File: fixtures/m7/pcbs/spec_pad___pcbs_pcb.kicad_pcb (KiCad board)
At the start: 2 copper layers, 3 parts

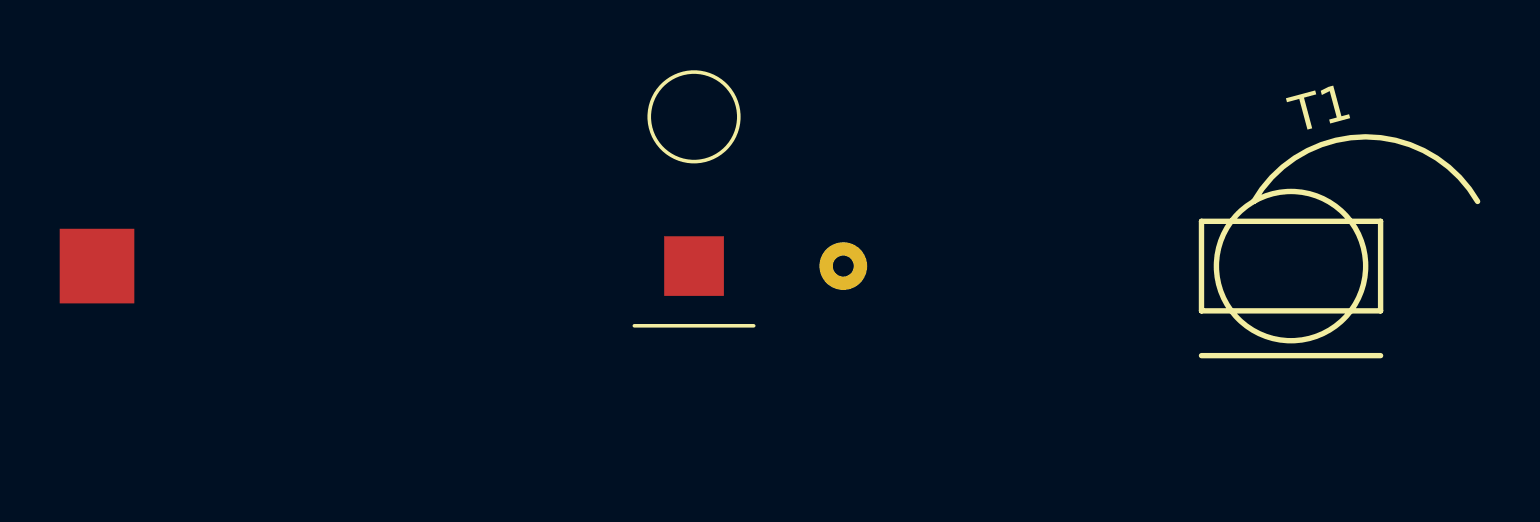
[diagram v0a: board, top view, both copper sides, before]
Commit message: Expand footprint specs and add JS footprints plan
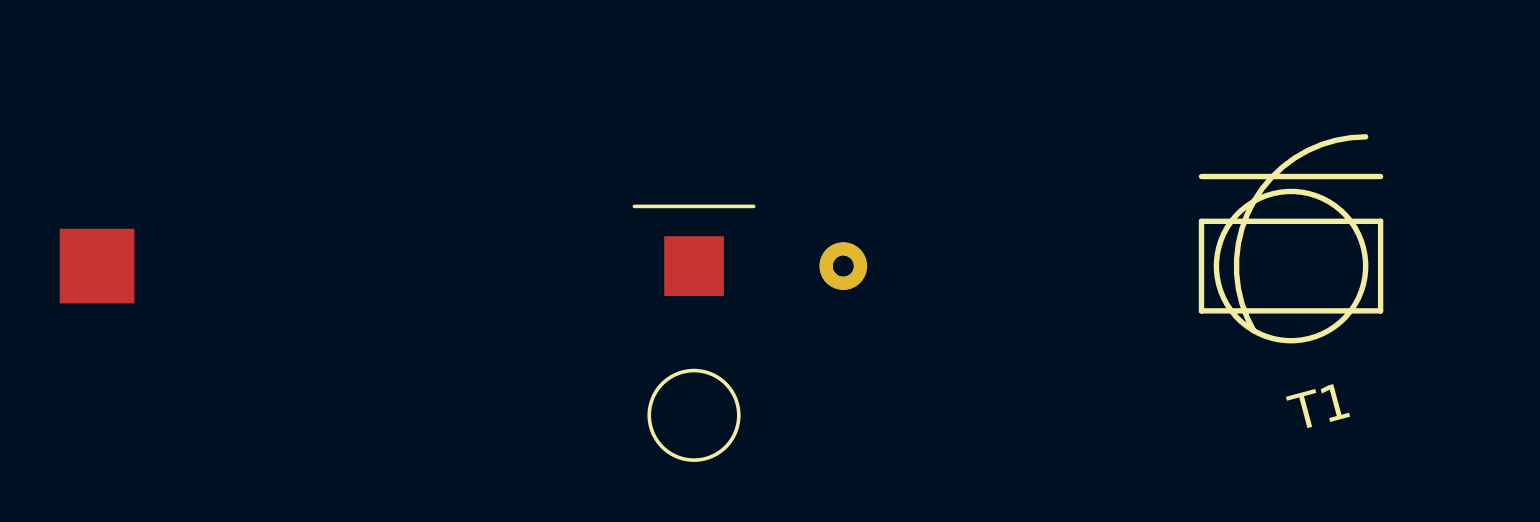
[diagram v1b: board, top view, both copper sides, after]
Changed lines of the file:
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@@
             (fp_text reference "FP1" (at 0 0) (layer F.SilkS) hide (effects (font (size 1.27 1.27) (thickness 0.15))))
             (fp_text value "" (at 0 0) (layer F.SilkS) hide (effects (font (size 1.27 1.27) (thickness 0.15))))
-            (pad 1 smd rect (at 0 0 0) (size 2.5 2.5) (layers F.Cu F.Mask) (net 1 "GND"))
+            (pad 1 smd rect (at 0 0) (size 2.5 2.5) (layers F.Cu F.Mask) (net 1 "GND"))
         )
         (module pad_primitives (layer F.Cu)
@@
             (fp_text reference "FP2" (at 0 0) (layer F.SilkS) hide (effects (font (size 1.27 1.27) (thickness 0.15))))
             (fp_text value "" (at 0 0) (layer F.SilkS) hide (effects (font (size 1.27 1.27) (thickness 0.15))))
-            (pad 1 smd rect (at 0 0 0) (size 2 2) (layers F.Cu F.Mask) (net 2 "VCC"))
-            (pad 2 thru_hole circle (at 5 0 0) (size 1.6 1.6) (drill 0.7) (layers F.Cu B.Cu F.Mask B.Mask) (net 2 "VCC"))
-            (fp_circle (center 0 -5) (end 1.5 -5) (layer F.SilkS) (width 0.12))
-            (fp_line (start -2 2) (end 2 2) (layer F.SilkS) (width 0.12))
+            (pad 1 smd rect (at 0 0) (size 2 2) (layers F.Cu F.Mask) (net 2 "VCC"))
+            (pad 2 thru_hole circle (at 5 0) (size 1.6 1.6) (drill 0.7) (layers F.Cu B.Cu F.Mask B.Mask) (net 2 "VCC"))
+            (fp_circle (center 0 5) (end 1.5 5) (layer F.SilkS) (width 0.12))
+            (fp_line (start -2 -2) (end 2 -2) (layer F.SilkS) (width 0.12))
         )
         (module primitives_templated (layer F.Cu)
@@
             (fp_text value "" (at 0 0) (layer F.SilkS) hide (effects (font (size 1.27 1.27) (thickness 0.15))))
             (fp_circle (center 0 0) (end 2.5 0) (layer F.SilkS) (width 0.18))
-            (fp_line (start -3 3) (end 3 3) (layer F.SilkS) (width 0.18))
-            (fp_arc (start 2.5 0) (end -1.2499999999999996 -2.165063509461097) (angle 120) (layer F.SilkS) (width 0.18))
-            (fp_line (start -3 1.5) (end 3 1.5) (layer F.SilkS) (width 0.18))
-            (fp_line (start 3 1.5) (end 3 -1.5) (layer F.SilkS) (width 0.18))
-            (fp_line (start 3 -1.5) (end -3 -1.5) (layer F.SilkS) (width 0.18))
-            (fp_line (start -3 -1.5) (end -3 1.5) (layer F.SilkS) (width 0.18))
-            (fp_text user "T1" (at 0 -5 15) (layer F.SilkS) (effects (font (size 1.2 1.2) (thickness 0.18)) (justify left)))
+            (fp_line (start -3 -3) (end 3 -3) (layer F.SilkS) (width 0.18))
+            (fp_arc (start 2.5 0) (end -1.2499999999999996 2.165063509461097) (angle 120) (layer F.SilkS) (width 0.18))
+            (fp_line (start -3 -1.5) (end 3 -1.5) (layer F.SilkS) (width 0.18))
+            (fp_line (start 3 -1.5) (end 3 1.5) (layer F.SilkS) (width 0.18))
+            (fp_line (start 3 1.5) (end -3 1.5) (layer F.SilkS) (width 0.18))
+            (fp_line (start -3 1.5) (end -3 -1.5) (layer F.SilkS) (width 0.18))
+            (fp_text user "T1" (at 0 5 15) (layer F.SilkS) (effects (font (size 1.2 1.2) (thickness 0.18)) (justify left)))
         )
 )
